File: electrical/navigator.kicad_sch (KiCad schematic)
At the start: 0 parts

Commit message: Added Transponder and Navigator
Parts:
- added GAD29: ~, symbol flyerx:Garmin_GAD29
- added GPS175: ~, symbol flyerx:Garmin_GPS175
- added GPS175_CONFIG: ~, symbol flyerx:Garmin_Config
- added WAAS_GPS_ANT: Antenna, symbol Device:Antenna
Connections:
- new net: GPS175.P1751_23 (CONFIG_MODULE_GROUND), GPS175_CONFIG.BLK (GND)
- new net: GPS175.P1751_43 (CONFIG_MODULE_POWER_OUT), GPS175_CONFIG.RED (VCC)
- new net: GPS175.P1751_1 (CONFIG_MODULE_CLOCK), GPS175_CONFIG.WHT (CLK)
- new net: GPS175.P1751_22 (CONFIG_MODULE_DATA), GPS175_CONFIG.YLW (DATA)
- new net: GPS175.GPS (GPS_ANTENNA), WAAS_GPS_ANT.1 (A)
- new net: GAD29.P292_11 (ARINC_RX_1B), GPS175.P1751_6 (ARINC_429_1_TX_B)
- new net: GAD29.P292_12 (ARINC_TX_1B), GPS175.P1751_28 (ARINC_429_1_RX_B)
- new net: GAD29.P292_23 (ARINC_RX_1A), GPS175.P1751_5 (ARINC_429_1_TX_A)
- new net: GAD29.P292_24 (ARINC_TX_1A), GPS175.P1751_27 (ARINC_429_1_RX_A)
- new net ADSB_ETHERNET_IN_A: GPS175.P1751_11 (ETHERNET_RX_P)
- new net ADSB_ETHERNET_IN_B: GPS175.P1751_33 (ETHERNET_RX_N)
- new net ADSB_ETHERNET_OUT_A: GPS175.P1751_10 (ETHERNET_TX_P)
- new net ADSB_ETHERNET_OUT_B: GPS175.P1751_32 (ETHERNET_TX_N)
- new net CAN_HI_IN: GAD29.P291_1 (CAN_HI)
- new net CAN_LO_IN: GAD29.P291_2 (CAN_LO)
- new net CONNEXT_SERIAL_GND: GPS175.P1751_51 (RS-232_2_GND)
- new net CONNEXT_SERIAL_IN: GPS175.P1751_30 (RS-232_2_RX)
- new net CONNEXT_SERIAL_OUT: GPS175.P1751_8 (RS-232_2_TX)
- new net ELT_SERIAL_GND: GPS175.P1751_50 (RS-232_3_GND)
- new net ELT_SERIAL_OUT: GPS175.P1751_7 (RS-232_3_TX)
- new net GAD29_BAK_PWR: GAD29.P291_8 (AIRCRAFT_POWER_2)
- new net GAD29_PWR: GAD29.P291_7 (AIRCRAFT_POWER_1)
- new net GND: GAD29.P291_9 (POWER_GROUND), GPS175.P1751_20 (POWER_GND), GPS175.P1751_41 (POWER_GND), GPS175.P1751_61 (REMOTE_POWER_ON)
- new net GPS175_BAK_PWR: GPS175.P1751_42 (POWER_INPUT_2)
- new net GPS175_PWR: GPS175.P1751_21 (POWER_INPUT_1)
- new net LIGHTING_HI: GPS175.P1751_19 (LIGHTING_BUS_HI)
- new net LIGHTING_LO: GPS175.P1751_40 (LIGHTING_BUS_LO)
- new net MAPMX_SERIAL_GND: GPS175.P1751_52 (RS-232_1_GND)
- new net MAPMX_SERIAL_IN: GPS175.P1751_31 (RS-232_1_RX)
- new net MAPMX_SERIAL_OUT: GPS175.P1751_9 (RS-232_1_TX)
- no-connect marks 0 -> 2
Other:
- note added: "Connext 57600"
- note added: "EFIS/AirData"
- note added: "EFIS/AirData Nav 1, Low Speed"
- note added: "Gama Format 1"
- note added: "Garmin GPS Nav 1, Low Speed"
- note added: "MapMX"
- note added: "NMEA"

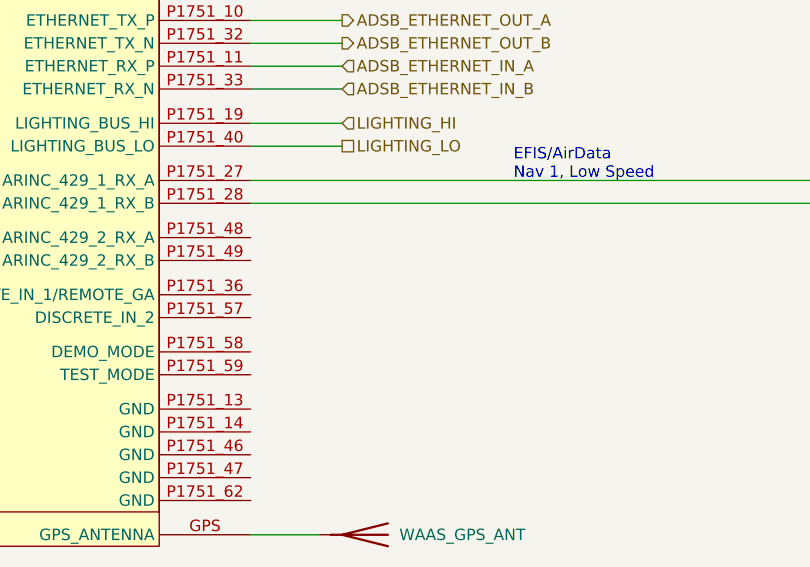
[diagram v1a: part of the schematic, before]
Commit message: Added autopilot
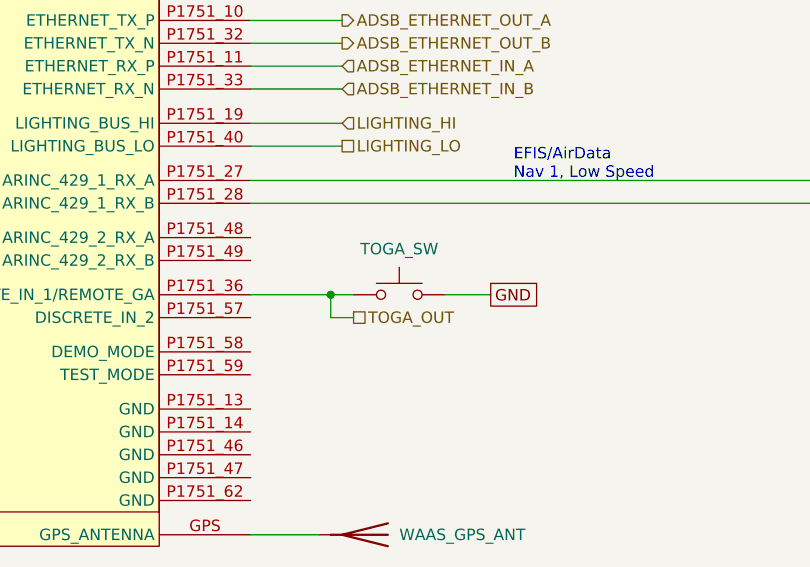
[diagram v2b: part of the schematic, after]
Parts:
- added TOGA_SW: SW_Push, symbol Switch:SW_Push
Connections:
- net GND: now also TOGA_SW.2
- net TOGA_OUT: now reaches GPS175.P1751_36 (DISCRETE_IN_1/REMOTE_GA)
- net TOGA_OUT: now also TOGA_SW.1
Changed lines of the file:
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@@
   (junction (at 153.67 34.29) (diameter 0) (color 0 0 0 0)
+  )
+  (junction (at 73.66 172.72) (diameter 0) (color 0 0 0 0)
   )
   (junction (at 68.58 26.67) (diameter 0) (color 0 0 0 0)
@@
     (stroke (width 0) (type default))
   )
+  (wire (pts (xy 64.77 172.72) (xy 73.66 172.72))
+    (stroke (width 0) (type default))
+  )
   (wire (pts (xy 64.77 147.32) (xy 74.93 147.32))
     (stroke (width 0) (type default))
@@
     (stroke (width 0) (type default))
   )
+  (wire (pts (xy 73.66 172.72) (xy 76.2 172.72))
+    (stroke (width 0) (type default))
+  )
   (wire (pts (xy 130.81 162.56) (xy 130.81 53.34))
     (stroke (width 0) (type default))
@@
     (stroke (width 0) (type default))
   )
+  (wire (pts (xy 73.66 175.26) (xy 73.66 172.72))
+    (stroke (width 0) (type default))
+  )
   (wire (pts (xy 64.77 24.13) (xy 72.39 24.13))
     (stroke (width 0) (type default))
@@
     (stroke (width 0) (type default))
   )
+  (wire (pts (xy 86.36 172.72) (xy 91.44 172.72))
+    (stroke (width 0) (type default))
+  )
   (wire (pts (xy 140.97 68.58) (xy 140.97 71.12))
     (stroke (width 0) (type default))
@@
   )
   (wire (pts (xy 129.54 48.26) (xy 158.75 48.26))
+    (stroke (width 0) (type default))
+  )
+  (wire (pts (xy 76.2 175.26) (xy 73.66 175.26))
     (stroke (width 0) (type default))
   )
@@
     )
   )
+  (global_label "GND" (shape passive) (at 91.44 172.72 0) (fields_autoplaced)
+    (effects (font (size 1.27 1.27)) (justify left))
+    (property "Intersheetrefs" "${INTERSHEET_REFS}" (at 97.1844 172.72 0)
+      (effects (font (size 1.27 1.27)) (justify left) hide)
+    )
+  )
   (global_label "GND" (shape passive) (at 148.59 27.94 180) (fields_autoplaced)
     (effects (font (size 1.27 1.27)) (justify right))
@@
   (hierarchical_label "GAD29_BAK_PWR" (shape input) (at 148.59 25.4 180) (fields_autoplaced)
     (effects (font (size 1.27 1.27)) (justify right))
+  )
+  (hierarchical_label "TOGA_OUT" (shape passive) (at 76.2 175.26 0) (fields_autoplaced)
+    (effects (font (size 1.27 1.27)) (justify left))
   )
   (symbol (lib_id "flyerx:Garmin_Config") (at 82.55 34.29 0) (mirror y) (unit 1)
@@
         )
       )
+    )
+  )
+  (symbol (lib_id "Switch:SW_Push") (at 81.28 172.72 0) (unit 1)
+    (in_bom yes) (on_board yes) (dnp no)
+    (property "Reference" "TOGA_SW" (at 81.28 167.64 0)
+      (effects (font (size 1.27 1.27)))
+    )
+    (property "Value" "SW_Push" (at 81.28 167.64 0)
+      (effects (font (size 1.27 1.27)) hide)
+    )
+    (property "Footprint" "" (at 81.28 167.64 0)
+      (effects (font (size 1.27 1.27)) hide)
+    )
+    (property "Datasheet" "~" (at 81.28 167.64 0)
+      (effects (font (size 1.27 1.27)) hide)
+    )
+    (pin "1")
+    (pin "2")
+    (instances
+      (project "electrical"
+        (path "/e8ec215a-dbe2-4eba-a577-e50a0a128049/a7d1a714-f940-4397-adef-d76b5058aa57"
+          (reference "TOGA_SW") (unit 1)
+        )
+      )

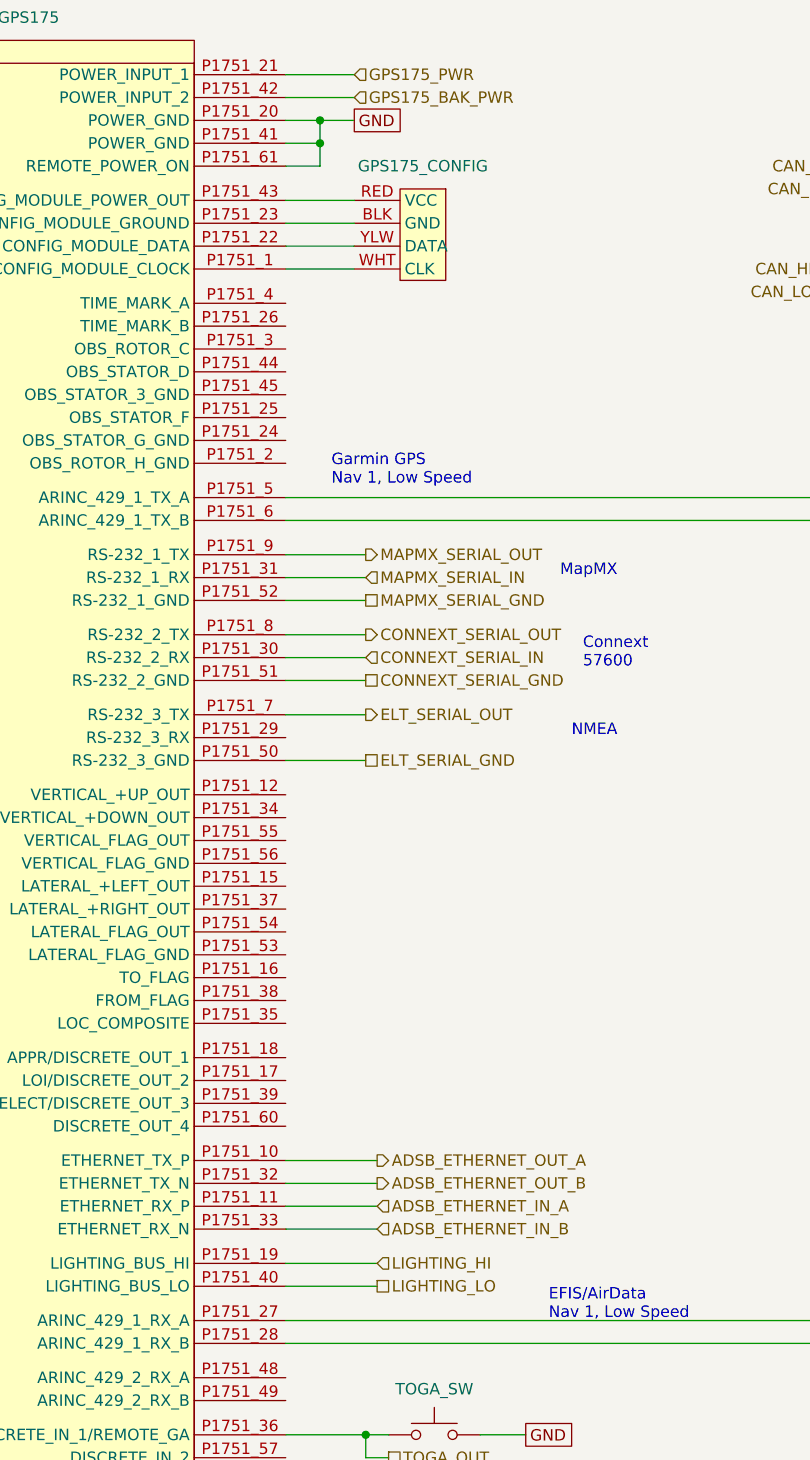
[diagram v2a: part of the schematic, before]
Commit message: Simplified lighting ground
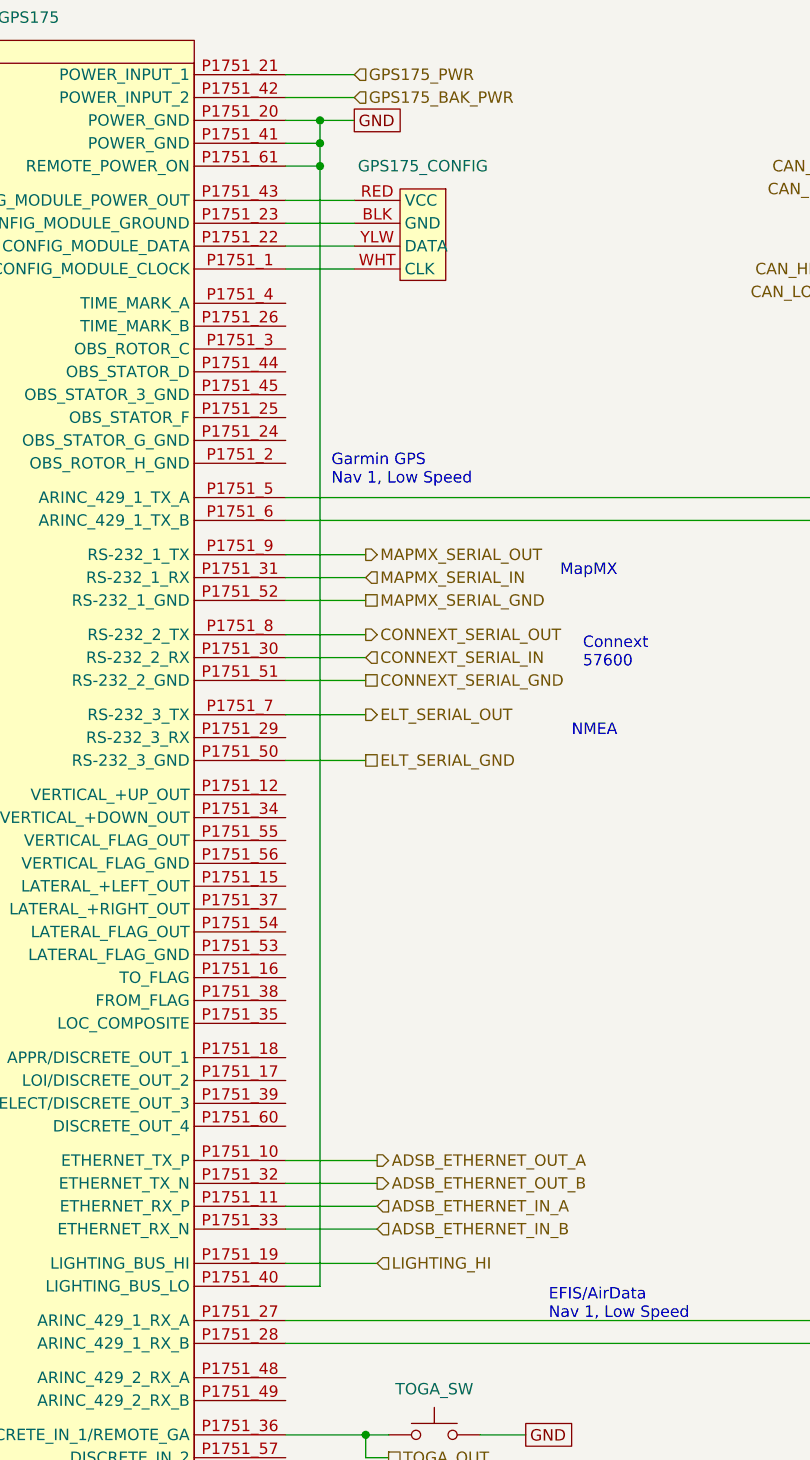
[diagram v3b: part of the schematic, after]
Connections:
- net LIGHTING_LO is gone; now on net GND: GPS175.P1751_40 (LIGHTING_BUS_LO)
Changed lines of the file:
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@@
 (kicad_sch (version 20230121) (generator eeschema)
   (paper "A" portrait)
+  (junction (at 68.58 31.75) (diameter 0) (color 0 0 0 0)
+  )
   (junction (at 152.4 31.75) (diameter 0) (color 0 0 0 0)
   )
@@
     (stroke (width 0) (type default))
   )
+  (wire (pts (xy 64.77 156.21) (xy 68.58 156.21))
+    (stroke (width 0) (type default))
+  )
   (wire (pts (xy 64.77 92.71) (xy 73.66 92.71))
     (stroke (width 0) (type default))
@@
     (stroke (width 0) (type default))
   )
+  (wire (pts (xy 68.58 156.21) (xy 68.58 31.75))
+    (stroke (width 0) (type default))
+  )
   (wire (pts (xy 64.77 68.58) (xy 140.97 68.58))
     (stroke (width 0) (type default))
@@
   )
   (wire (pts (xy 64.77 86.36) (xy 73.66 86.36))
-    (stroke (width 0) (type default))
-  )
-  (wire (pts (xy 64.77 156.21) (xy 74.93 156.21))
     (stroke (width 0) (type default))
   )
@@
     (effects (font (size 1.27 1.27)) (justify left))
   )
-  (hierarchical_label "LIGHTING_LO" (shape passive) (at 74.93 156.21 0) (fields_autoplaced)
-    (effects (font (size 1.27 1.27)) (justify left))
-  )

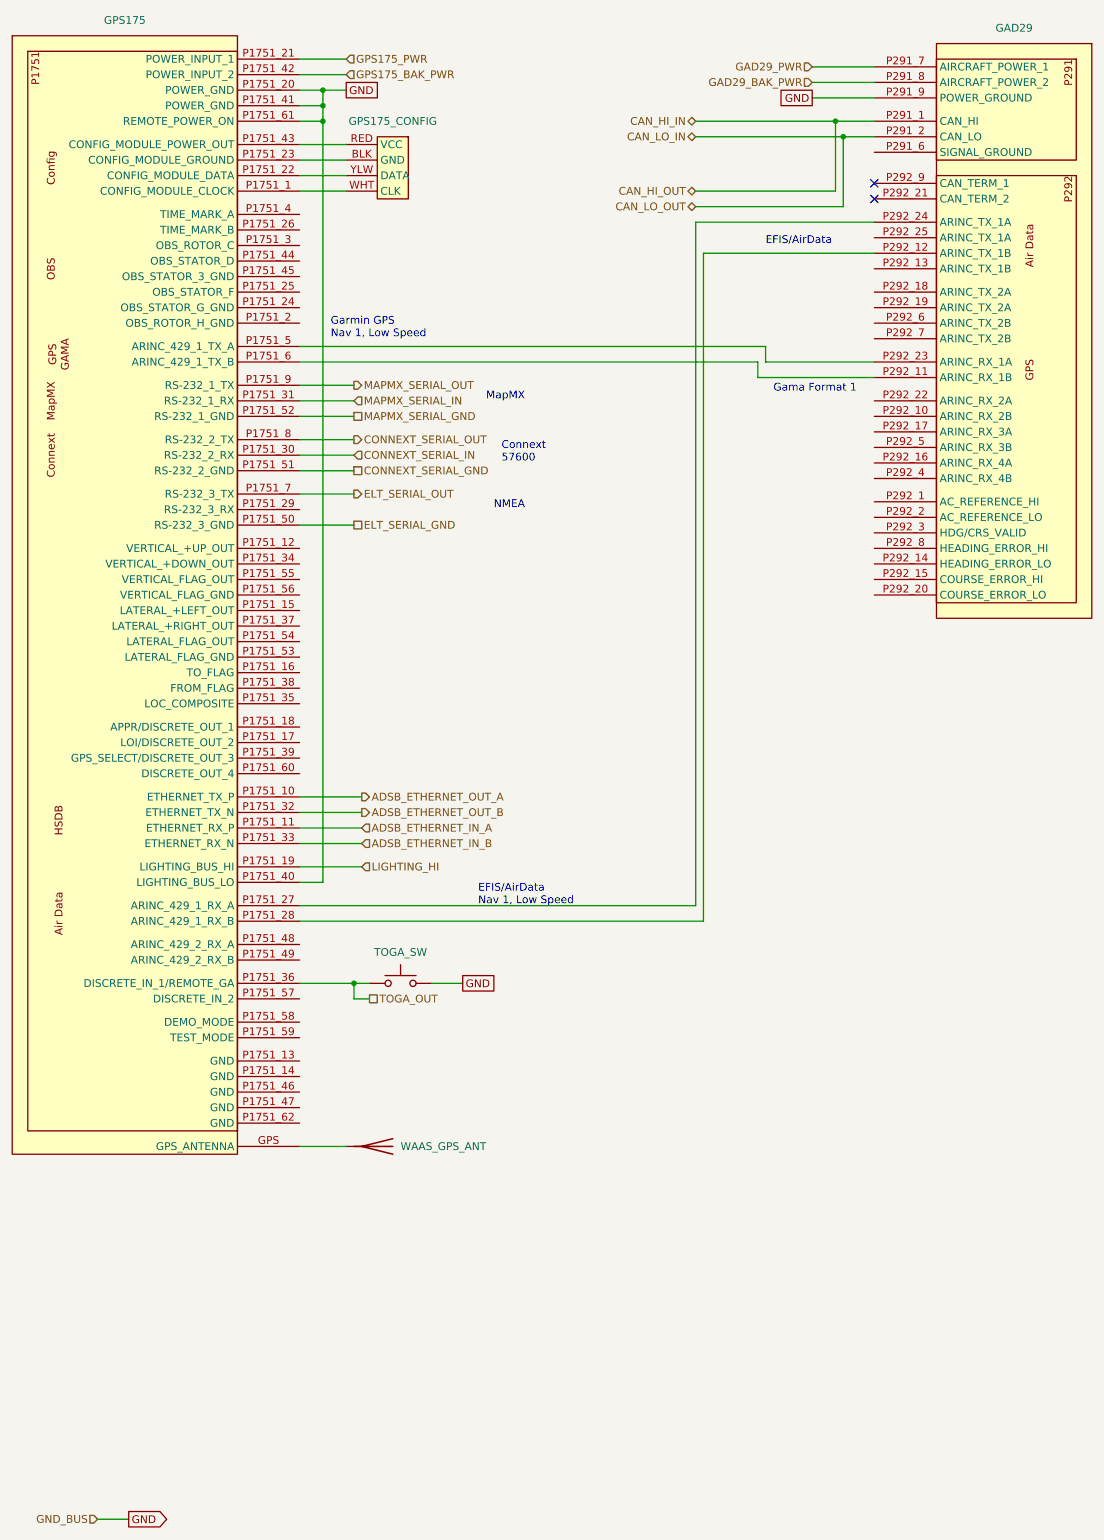
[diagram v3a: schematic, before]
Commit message: Updated settings for RS-232, etc.
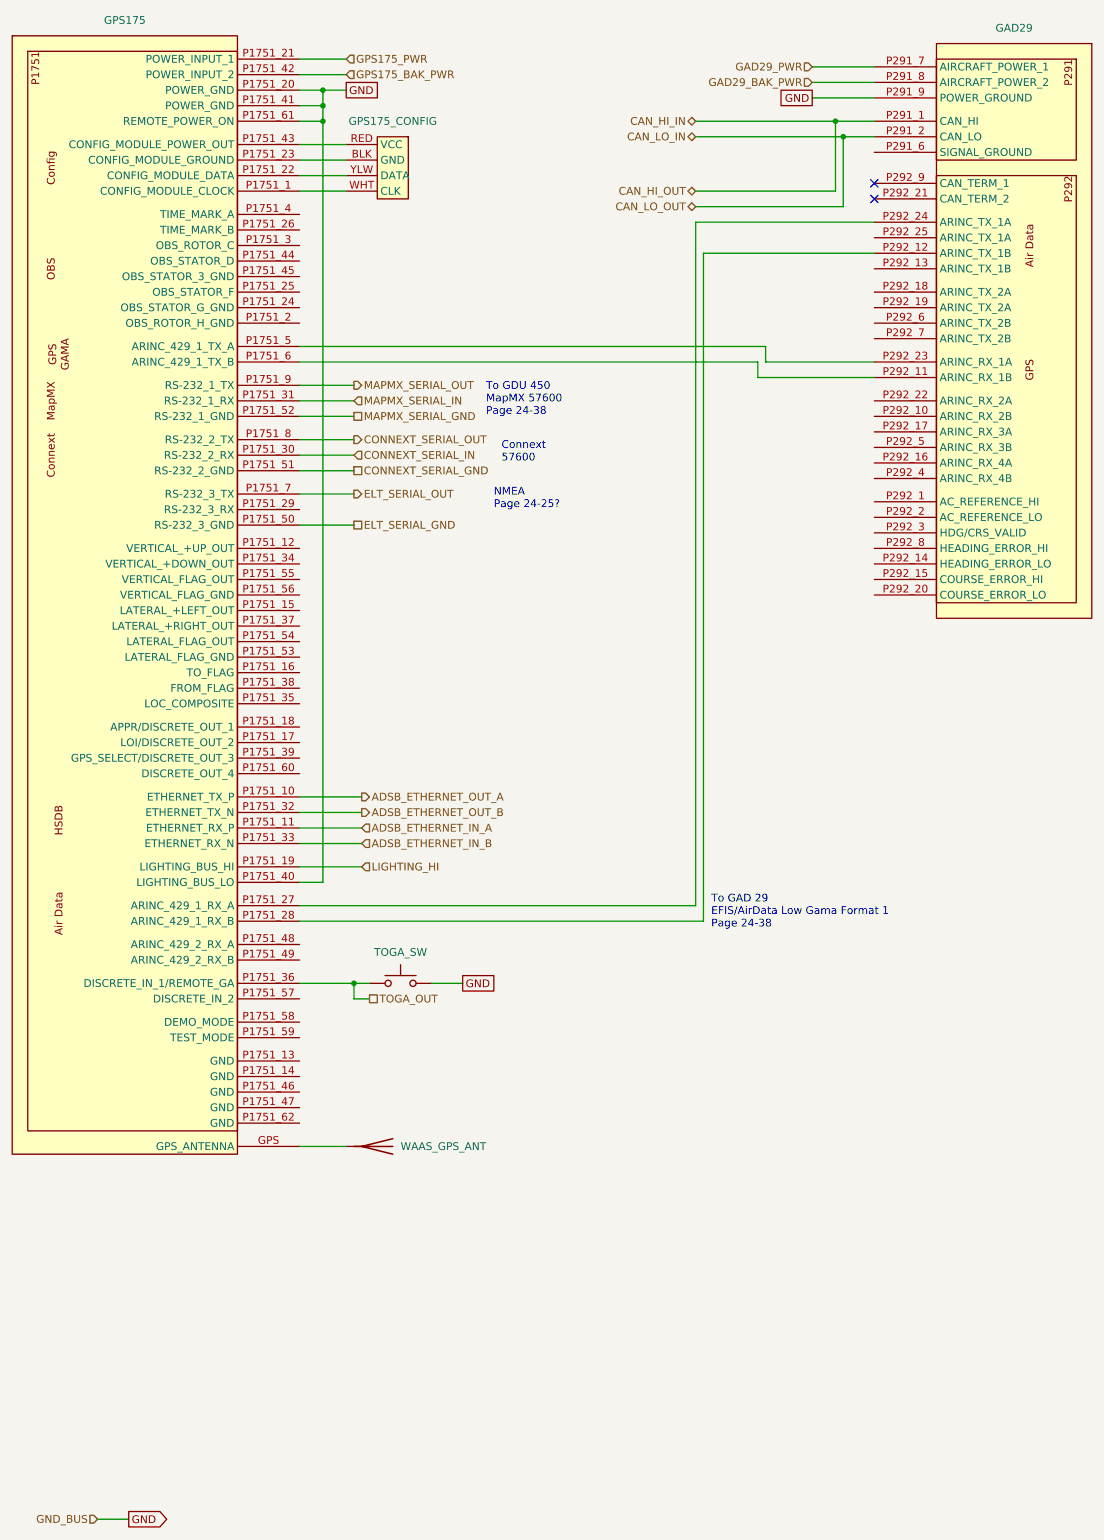
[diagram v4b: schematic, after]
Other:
- note added: "NMEA Page 24-25?"
- note added: "To GAD 29 EFIS/AirData Low Gama Format 1 Page 24-38"
- note added: "To GDU 450 MapMX 57600 Page 24-38"
- note removed: "EFIS/AirData"
- note removed: "EFIS/AirData Nav 1, Low Speed"
- note removed: "Gama Format 1"
- note removed: "Garmin GPS Nav 1, Low Speed"
- note removed: "MapMX"
- note removed: "NMEA"
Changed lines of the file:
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@@
     (stroke (width 0) (type default))
   )
-  (text "NMEA" (at 96.52 95.25 0)
+  (text "NMEA\nPage 24-25?" (at 96.52 95.25 0)
     (effects (font (size 1.27 1.27)) (justify left bottom))
   )
-  (text "MapMX" (at 95.25 77.47 0)
+  (text "To GDU 450\nMapMX 57600\nPage 24-38" (at 95.25 80.01 0)
     (effects (font (size 1.27 1.27)) (justify left bottom))
   )
@@
     (effects (font (size 1.27 1.27)) (justify left bottom))
   )
-  (text "Garmin GPS\nNav 1, Low Speed" (at 69.85 67.31 0)
+  (text "To GAD 29\nEFIS/AirData Low Gama Format 1\nPage 24-38"
+    (at 132.08 163.83 0)
     (effects (font (size 1.27 1.27)) (justify left bottom))
   )
-  (text "Gama Format 1" (at 142.24 76.2 0)
-    (effects (font (size 1.27 1.27)) (justify left bottom))
-  )
-  (text "EFIS/AirData" (at 140.97 52.07 0)
-    (effects (font (size 1.27 1.27)) (justify left bottom))
-  )
-  (text "EFIS/AirData \nNav 1, Low Speed" (at 93.98 160.02 0)
-    (effects (font (size 1.27 1.27)) (justify left bottom))
-  )
